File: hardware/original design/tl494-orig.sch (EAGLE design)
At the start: 79 parts, among them IC1 TL494CN, J1 CON_HEADER_1X02-PTH, K2 24V, Q1 2N5551, Q1I 8050, Q1I1 2N3904, Q2 8550, Q2I 8050, Q3 8050, Q4 2SK4145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

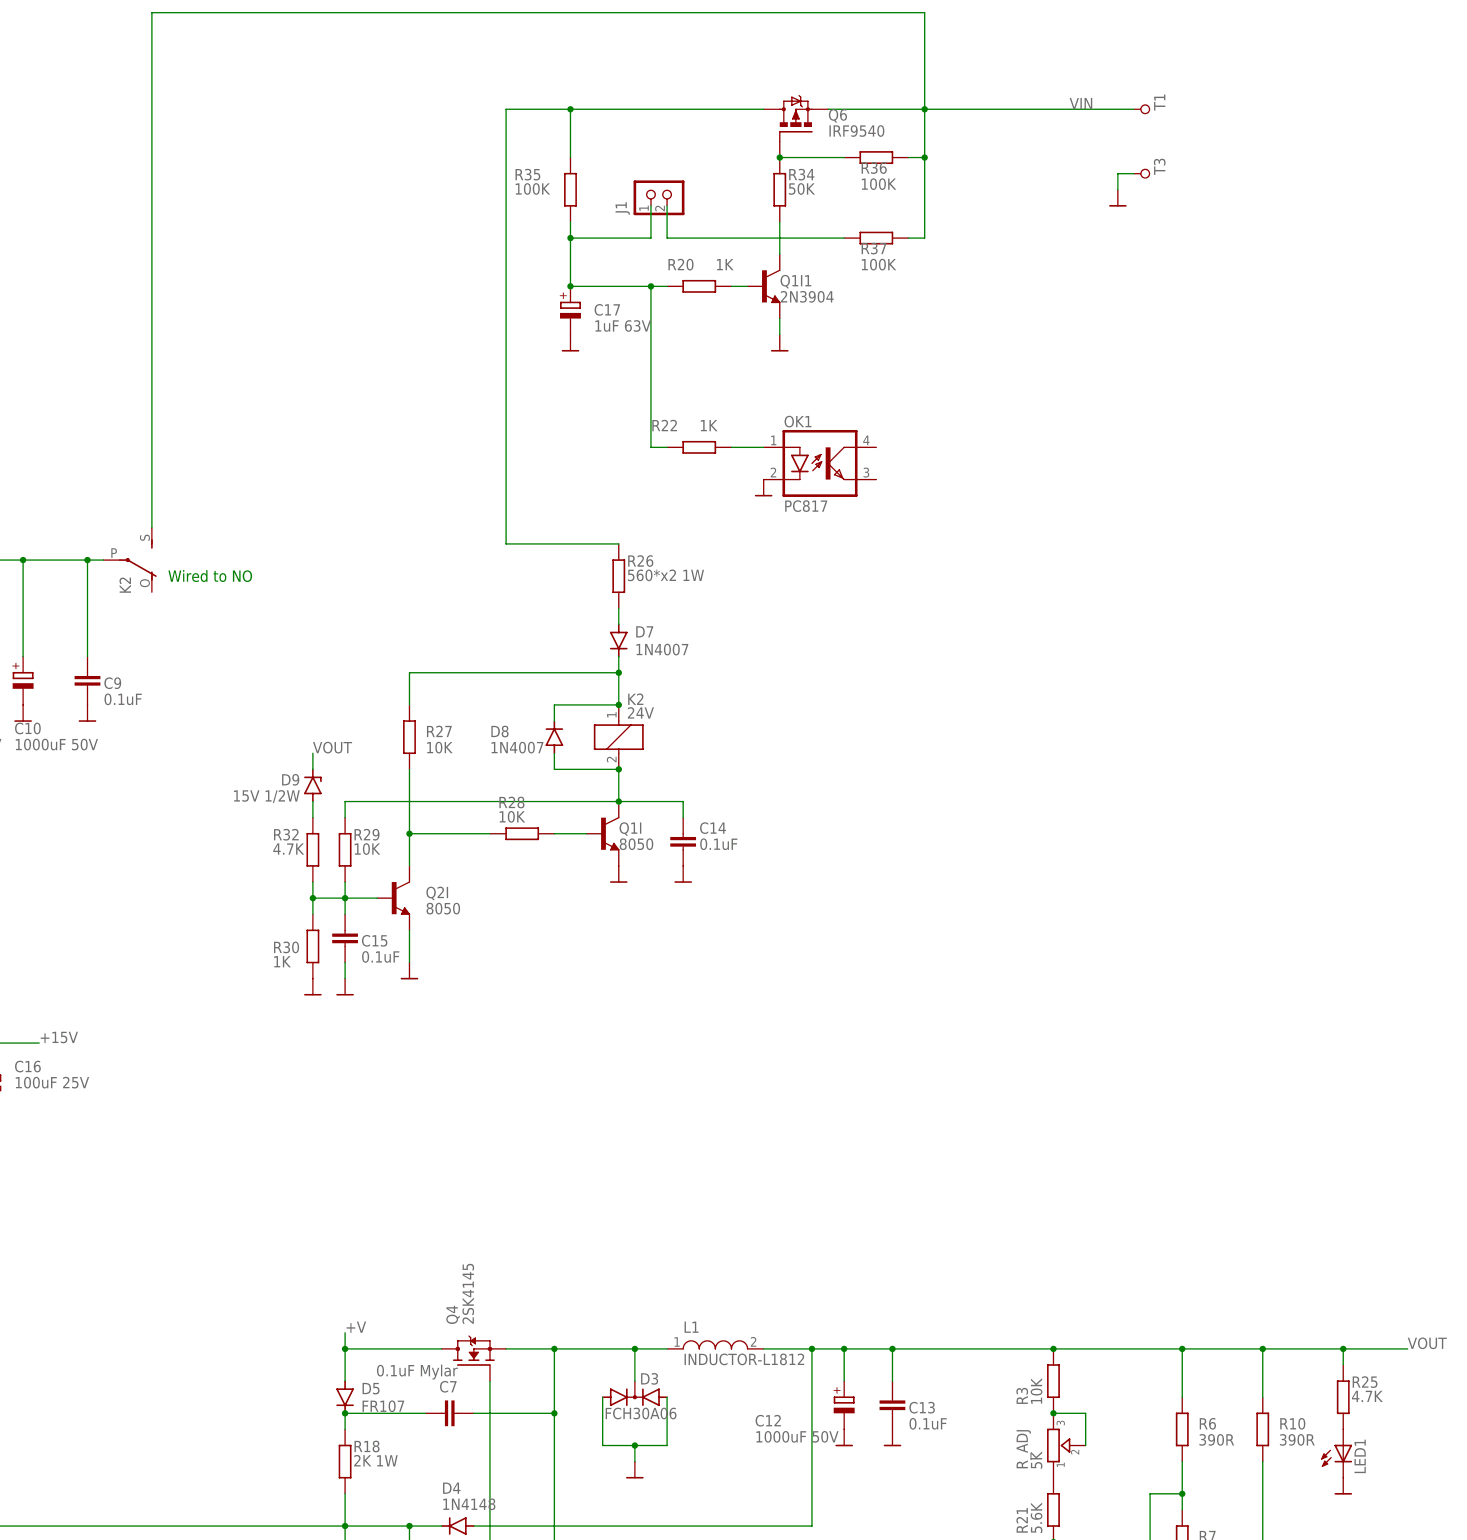
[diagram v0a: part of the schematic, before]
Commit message: partial board placement and started fix on latch swith problem
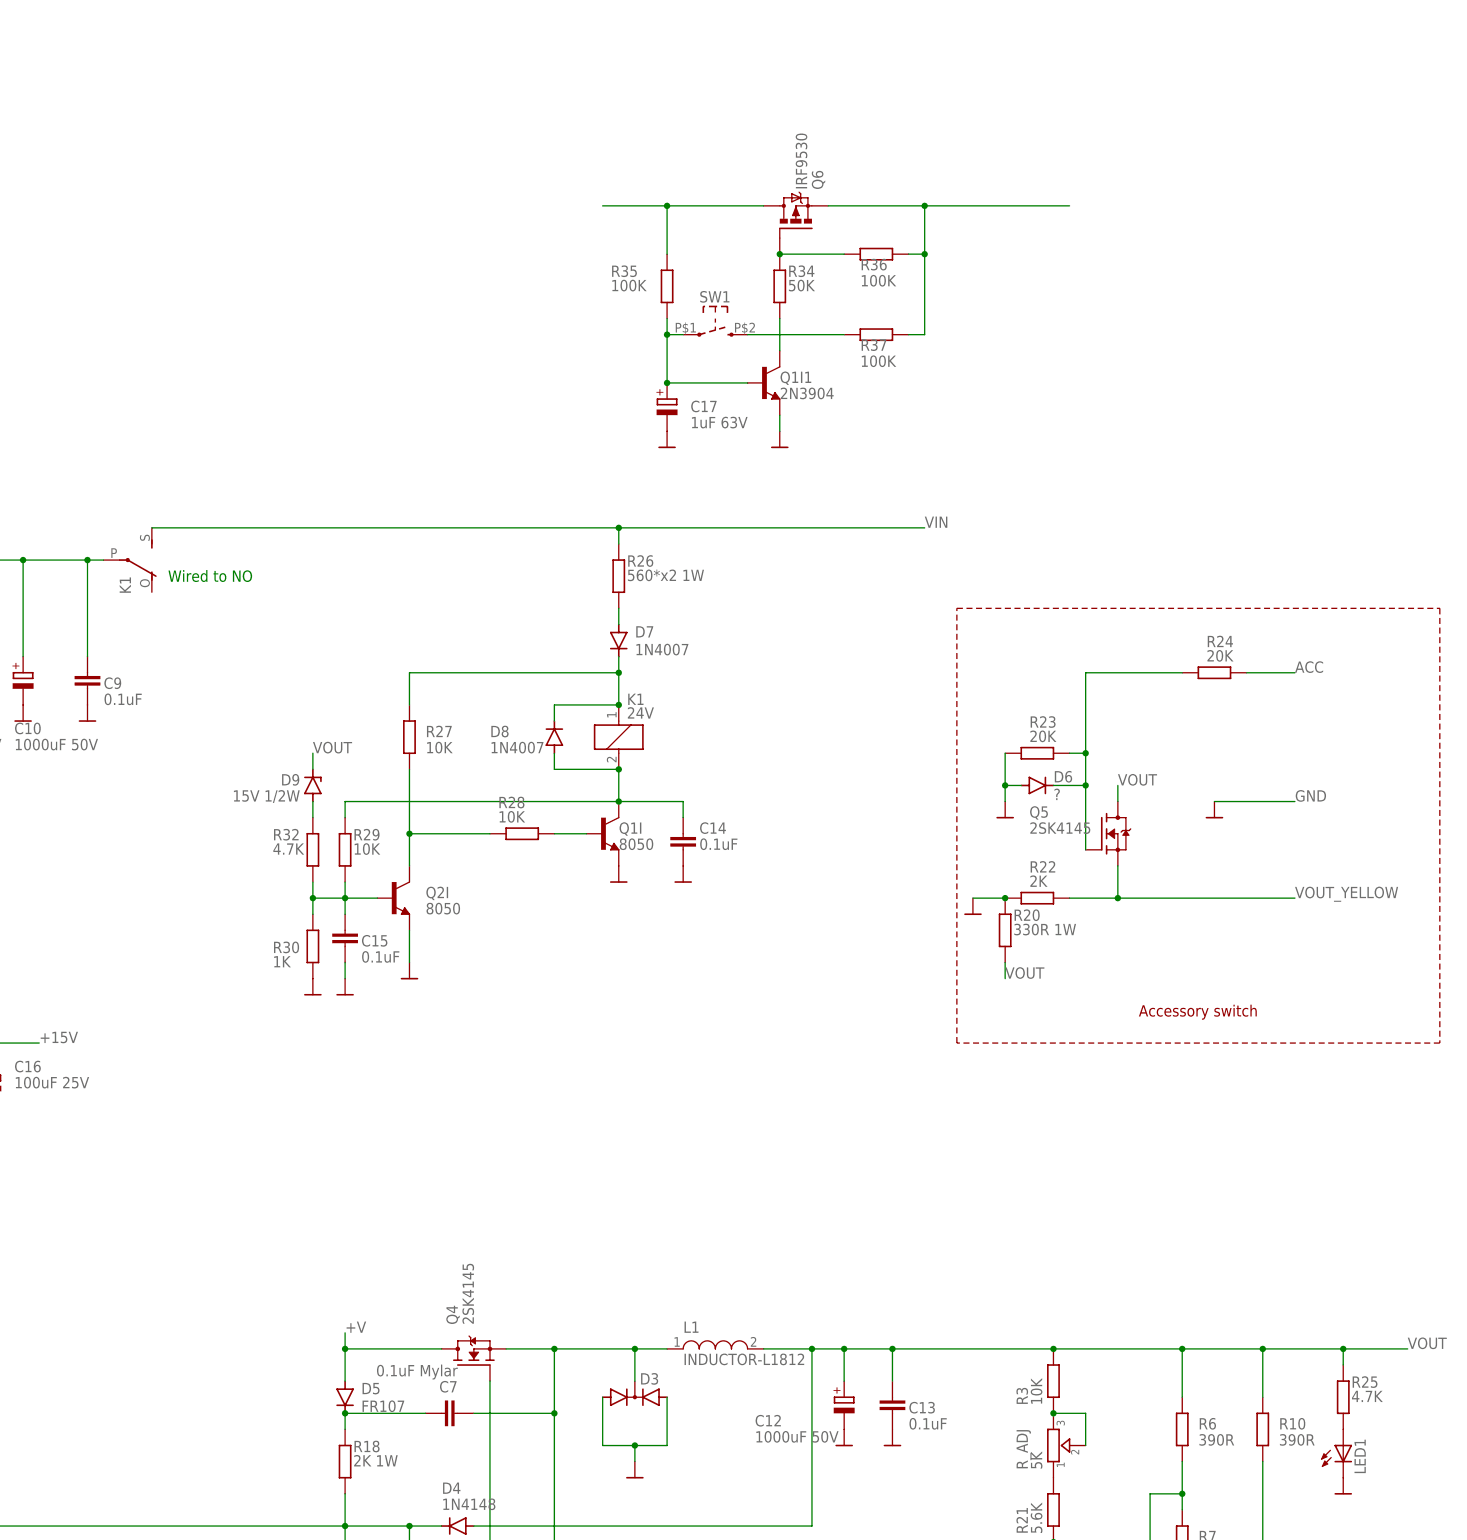
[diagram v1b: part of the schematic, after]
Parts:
- removed J1: CON_HEADER_1X02-PTH, dp_devices.v6:CON_HEADER_1X02-PTH
- removed K2: 24V, relay:G5L
- removed OK1: PC817, optocoupler:PC817
- removed T1: PAD_TERMINAL-1.02MM_ROUND, dp_devices.v6:PAD_TERMINAL-1.02MM_ROUND
- removed T3: PAD_TERMINAL-1.02MM_SQUARE, dp_devices.v6:PAD_TERMINAL-1.02MM_SQUARE
- added D6: ?, diode:1N4148DO35-10
- added K1: 24V, relay:G2R
- added Q5: 2SK4145, dp_devices.v6:TRANSISTOR_MOSFET-N-TO220V
- added R23, R24: 20K, rcl:R-EU_0207/10
- added SW1: SW_MEMBRANE, dp_devices.v6:SW_MEMBRANE
- C10, C11: device rcl:CPOL-EUE7.5-18 -> rcl:CPOL-EUE3.5-10
- C12: device rcl:CPOL-EUE5-13 -> rcl:CPOL-EUE3.5-10
- C17: device rcl:CPOL-EUE2-5 -> rcl:CPOL-EUE3.5-10
- D3: value FCH30A06 -> (none)
- Q6: value IRF9540 -> IRF9530
- R20: value 1K -> 330R 1W
- R22: value 1K -> 2K
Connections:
- removed net N$35: OK1.A, R22.1
- new net ACC: R24.2
- new net N$29: Q6.S, R36.1, R37.1
- new net VOUT_YELLOW: Q5.S, R22.2
- net +V: now also K12.P; no longer K22.P
- net GND: now also D6.A, R20.2, R22.1, R23.1; no longer OK1.C, T3.P
- net N$20: now also D6.C, Q5.G, R23.2, R24.1; no longer Q1I1.B, R20.1
- net N$23: now also K11.1; no longer K21.1
- net N$24: now also K11.2; no longer K21.2
- net N$32: no longer R26.2
- net N$33: now also Q1I1.B, SW1.1; no longer J1.1, R20.2, R22.2
- net N$34: now also SW1.2; no longer J1.2
- net VIN: now also K12.S, R26.2; no longer K22.S, Q6.S, R36.1, R37.1, T1.P
- net VOUT: now also Q5.D, R20.1
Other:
- note added: "Accessory switch"
- note removed: "Initial SW"
- note removed: "Latch circuit"
- moved on the sheet: C17, Q1I1, Q6, R20, R22, R34, R35, R36, R37
